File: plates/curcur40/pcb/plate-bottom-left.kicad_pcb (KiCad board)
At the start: 2 copper layers, 116.1 x 88.3 mm, 0 parts

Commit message: fix all
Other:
- board size 116.1 x 88.3 mm -> 125.1 x 92.6 mm
- rule pad_to_mask_clearance: 0.2 -> 0

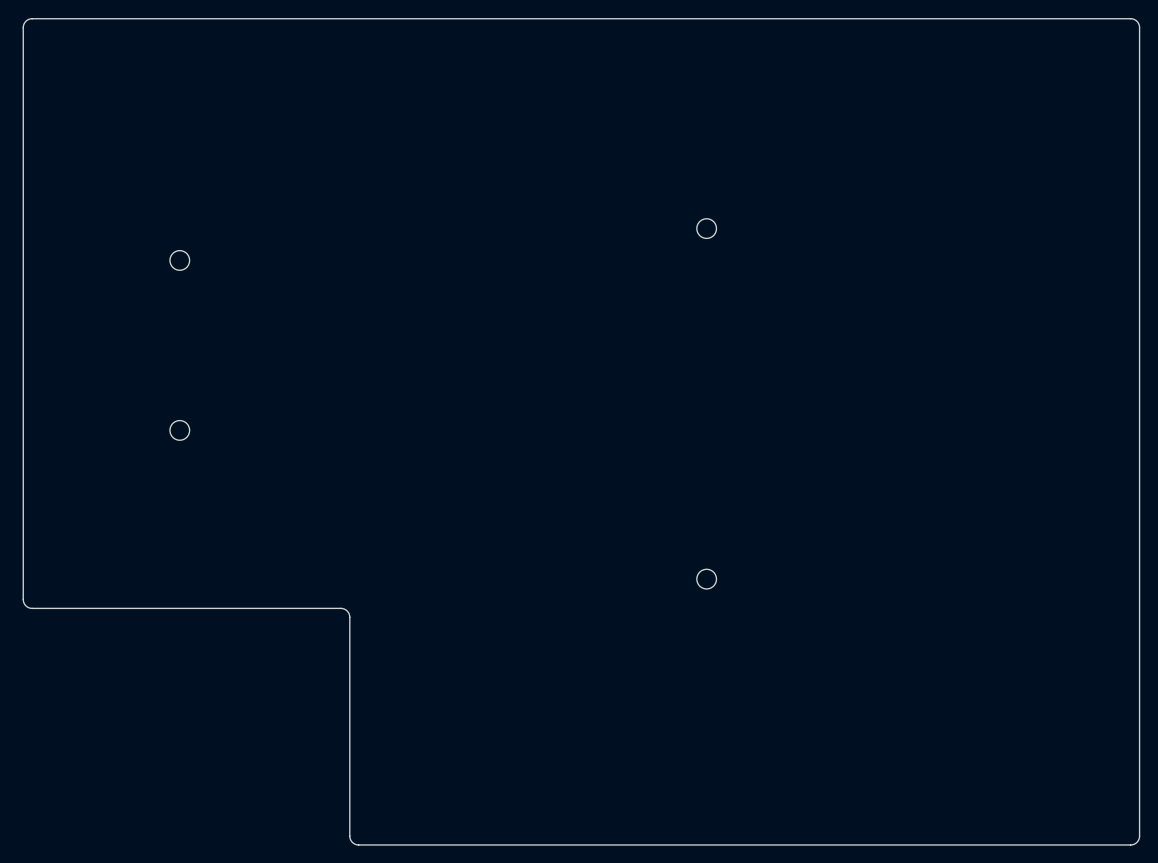
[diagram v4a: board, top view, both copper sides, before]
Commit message: Restore TRRS cutouts and relocate mounting holes to perimeter
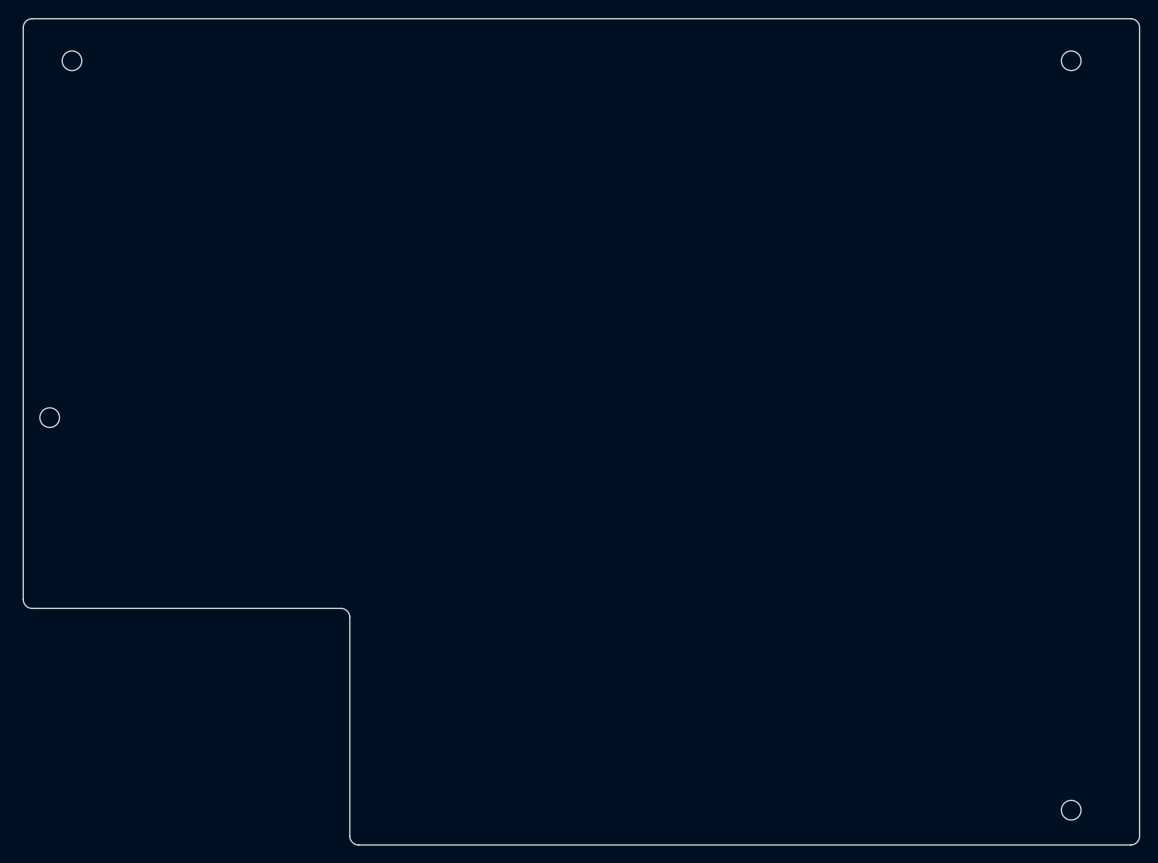
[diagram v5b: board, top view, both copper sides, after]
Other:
- outline, holes or cut-outs redrawn
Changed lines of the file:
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@@
 	)
 	(gr_circle
-		(center -101.9175 2.38125)
-		(end -100.8175 2.38125)
+		(center -116.5 20)
+		(end -115.4 20)
 		(stroke
 			(width 0.15)
@@
 	)
 	(gr_circle
-		(center -101.9175 21.43125)
-		(end -100.8175 21.43125)
+		(center -114 -20)
+		(end -112.9 -20)
 		(stroke
 			(width 0.15)
@@
 	)
 	(gr_circle
-		(center -42.8625 -1.190625)
-		(end -41.762499 -1.190625)
+		(center -2 -20)
+		(end -0.899999 -20)
 		(stroke
 			(width 0.15)
@@
 	)
 	(gr_circle
-		(center -42.8625 38.1)
-		(end -41.762499 38.1)
+		(center -2 64)
+		(end -0.899999 64)
 		(stroke
 			(width 0.15)

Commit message: fix trrs top plate
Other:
- outline, holes or cut-outs redrawn
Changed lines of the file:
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@@
 	)
 	(gr_circle
-		(center -116.5 20)
-		(end -115.4 20)
+		(center -100 -22.5)
+		(end -98.9 -22.5)
 		(stroke
 			(width 0.15)
@@
 	)
 	(gr_circle
-		(center -114 -20)
-		(end -112.9 -20)
+		(center -98 38)
+		(end -96.9 38)
 		(stroke
 			(width 0.15)
@@
 	)
 	(gr_circle
-		(center -2 -20)
-		(end -0.899999 -20)
+		(center -23.8125 -22.5)
+		(end -22.7125 -22.5)
 		(stroke
 			(width 0.15)
@@
 	)
 	(gr_circle
-		(center -2 64)
-		(end -0.899999 64)
+		(center -23.8125 64)
+		(end -22.7125 64)
 		(stroke
 			(width 0.15)
